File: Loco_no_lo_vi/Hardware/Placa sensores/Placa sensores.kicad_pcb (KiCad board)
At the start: 2 copper layers, 17 parts, among them J1 Conn_01x06_Female, U1 CNY70, U2 CNY70, U3 CNY70, U4 CNY70, U5 CNY70, U6 CNY70, U7 4053

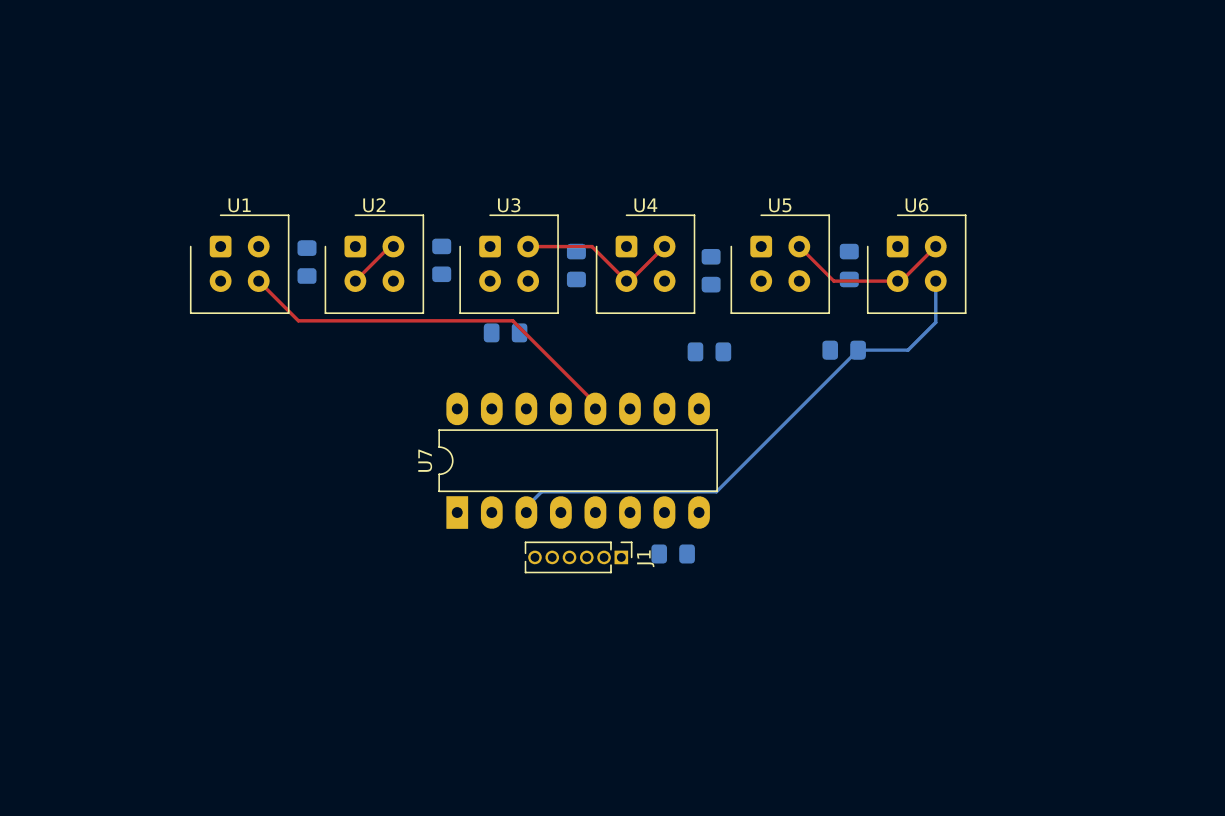
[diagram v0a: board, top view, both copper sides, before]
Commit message: Terminé de enrutar y no he puesto los tornillos
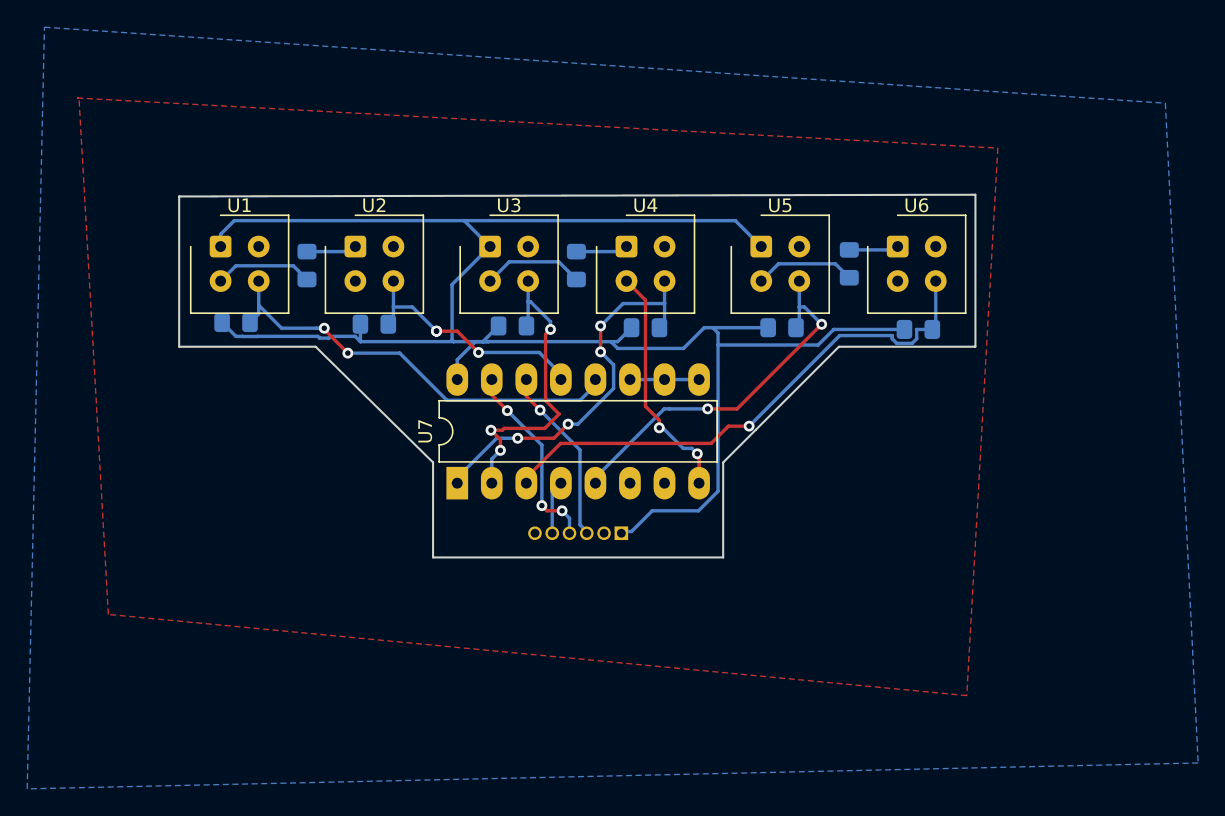
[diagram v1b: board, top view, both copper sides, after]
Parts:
- J1: moved to B.Cu
- moved R3 34.9 mm to (154.3, 46.2), turned to 0 degrees
- moved R9 18.5 mm to (194.4, 46.6), turned to 0 degrees
- moved R2 6.83 mm to (164.5, 46.4), turned to 0 degrees
- moved R5 6.39 mm to (184.4, 46.6), turned to 0 degrees
- moved R8 5.67 mm to (204.5, 46.7)
- moved U7 2.16 mm to (170.6, 58.0)
- moved J1 1.78 mm to (182.6, 61.7), turned to 90 degrees
- moved R6 0.72 mm to (174.6, 46.5)
- moved R1 0.25 mm to (159.5, 42.0), turned to 90 degrees
- moved R7 0.13 mm to (199.4, 41.9), turned to 90 degrees
- turned R4 to 90 degrees
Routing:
- net +5V: track 0.00 -> 138.3 mm
- net /sensor4: track 0.00 -> 28.6 mm, vias 0 -> 4
- net /sensor5: track 0.00 -> 27.4 mm, vias 0 -> 2
- net /sensor3: track 0.00 -> 22.9 mm, vias 0 -> 3
- net /sensor2: track 0.00 -> 18.1 mm, vias 0 -> 3
- net /linea2: track 0.00 -> 14.2 mm, vias 0 -> 3
- net /linea1: track 0.00 -> 13.0 mm, vias 0 -> 1
- net GND: track 28.1 -> 18.4 mm, vias 0 -> 2
- net Net-(R4-Pad1): track 0.00 -> 7.47 mm
- net Net-(R7-Pad1): track 0.00 -> 7.43 mm
- net Net-(R1-Pad1): track 0.00 -> 7.23 mm
- net /linea_selc: track 0.00 -> 5.08 mm
- net Net-(R4-Pad2): track 0.00 -> 3.84 mm
- net /linea3: track 0.00 -> 3.82 mm
- net Net-(R1-Pad2): track 0.00 -> 3.71 mm
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- added copper zone on B.Cu, net GND
- added copper zone on F.Cu, net GND
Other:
- board outline added: 58.5 x 26.7 mm
- board text added: "5v"
- board text added: "gnd"
- board text added: "loco_ni_lo_vi"
